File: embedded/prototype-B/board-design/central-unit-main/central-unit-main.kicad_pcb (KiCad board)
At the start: 2 copper layers, 45 x 92.5 mm, 96 parts, among them IC1 VEML6030, J1 Screw_Terminal_01x02, J2 2171790001, J3 Conn_02x05_Odd_Even, J4 Conn_ARM_JTAG_SWD_20, SW1 CAS-120TA1, U1 STM32L452RETx, U2 TPS63000, U3 MIC2778-2YM5-TR, U4 USBLC6-2SC6, U5 BQ24074RGT, U6 LIS2HH12, Y1 ECS-_327-12_5-34B-TR, Y2 STDCSU1-8M

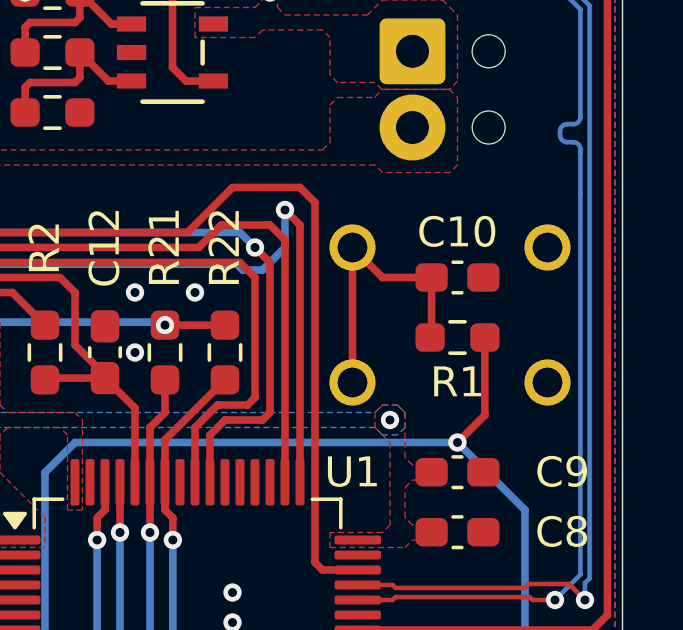
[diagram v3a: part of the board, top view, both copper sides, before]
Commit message: [Central unit] Tactile switch button wrongly routed
Fixed the MCU reset tactile switch bug.

Signed-off-by: Nicolae-Andrei Prodan <vasilenicolaeandrei@gmail.com>
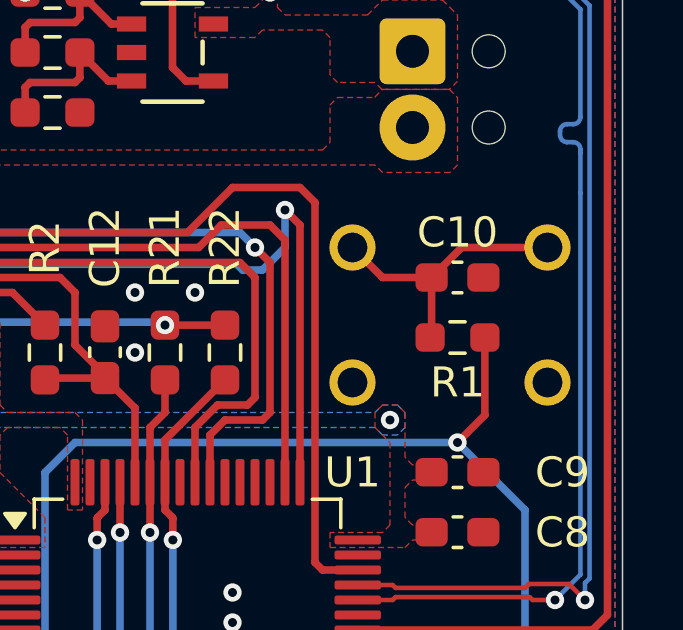
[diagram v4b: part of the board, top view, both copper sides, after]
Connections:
- C10 pad 1: Net-(S1-COM_2) -> Net-(S1-COM_1)
- R1 pad 1: Net-(S1-COM_2) -> Net-(S1-COM_1)
- S1 pad 1: GND -> Net-(S1-COM_1)
- S1 pad 2: Net-(S1-COM_2) -> Net-(S1-COM_1)
- S1 pad 4: Net-(S1-COM_2) -> GND
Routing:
- net Net-(S1-COM_2): track 9.57 -> 0.00 mm
- net Net-(S1-COM_1): track 0.00 -> 9.35 mm
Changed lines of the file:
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@@
 			(layers "F.Cu" "F.Mask" "F.Paste")
 			(roundrect_rratio 0.25)
-			(net "Net-(S1-COM_2)")
+			(net "Net-(S1-COM_1)")
 			(pintype "passive")
 		)
@@
 			(layers "F.Cu" "F.Mask" "F.Paste")
 			(roundrect_rratio 0.25)
-			(net "Net-(S1-COM_2)")
+			(net "Net-(S1-COM_1)")
 			(pintype "passive")
 		)
@@
 			(layers "*.Cu" "*.Mask")
 			(remove_unused_layers no)
-			(net "GND")
+			(net "Net-(S1-COM_1)")
 			(pinfunction "COM_1_1")
 			(pintype "passive")
@@
 			(layers "*.Cu" "*.Mask")
 			(remove_unused_layers no)
-			(net "Net-(S1-COM_2)")
+			(net "Net-(S1-COM_1)")
 			(pinfunction "COM_2_2")
 			(pintype "passive")
@@
 			(layers "*.Cu" "*.Mask")
 			(remove_unused_layers no)
-			(net "Net-(S1-COM_2)")
+			(net "GND")
 			(pinfunction "NO_2_4")
 			(pintype "passive")
@@
 	)
 	(segment
-		(start 155.5 86.5)
-		(end 155.5 91)
-		(width 0.254)
-		(locked yes)
-		(layer "F.Cu")
-		(net "Net-(S1-COM_2)")
-	)
-	(segment
-		(start 158.1375 87.5)
-		(end 158.1375 89.45)
-		(width 0.254)
-		(locked yes)
-		(layer "F.Cu")
-		(net "Net-(S1-COM_2)")
-	)
-	(segment
-		(start 158.1375 89.45)
-		(end 158.0875 89.5)
-		(width 0.254)
-		(locked yes)
-		(layer "F.Cu")
-		(net "Net-(S1-COM_2)")
-	)
-	(segment
-		(start 158.1375 87.5)
-		(end 156.5 87.5)
-		(width 0.254)
-		(locked yes)
-		(layer "F.Cu")
-		(net "Net-(S1-COM_2)")
-	)
-	(segment
-		(start 156.5 87.5)
-		(end 155.5 86.5)
-		(width 0.254)
-		(locked yes)
-		(layer "F.Cu")
-		(net "Net-(S1-COM_2)")
-	)
-	(segment
 		(start 131.5875 112)
 		(end 131.5875 117.9125)
@@
 		(net "/Connector/JTDO{slash}TRACESWO")
 	)
+	(segment
+		(start 158.1375 87.5)
+		(end 158.1375 89.45)
+		(width 0.254)
+		(layer "F.Cu")
+		(net "Net-(S1-COM_1)")
+	)
+	(segment
+		(start 159.1375 86.5)
+		(end 158.1375 87.5)
+		(width 0.254)
+		(layer "F.Cu")
+		(net "Net-(S1-COM_1)")
+	)
+	(segment
+		(start 158.1375 89.45)
+		(end 158.0875 89.5)
+		(width 0.254)
+		(layer "F.Cu")
+		(net "Net-(S1-COM_1)")
+	)
+	(segment
+		(start 162 86.5)
+		(end 159.1375 86.5)
+		(width 0.254)
+		(layer "F.Cu")
+		(net "Net-(S1-COM_1)")
+	)
+	(segment
+		(start 158.1375 87.5)
+		(end 156.5 87.5)
+		(width 0.254)
+		(layer "F.Cu")
+		(net "Net-(S1-COM_1)")
+	)
+	(segment
+		(start 156.5 87.5)
+		(end 155.5 86.5)
+		(width 0.254)
+		(layer "F.Cu")
+		(net "Net-(S1-COM_1)")
+	)
 	(zone

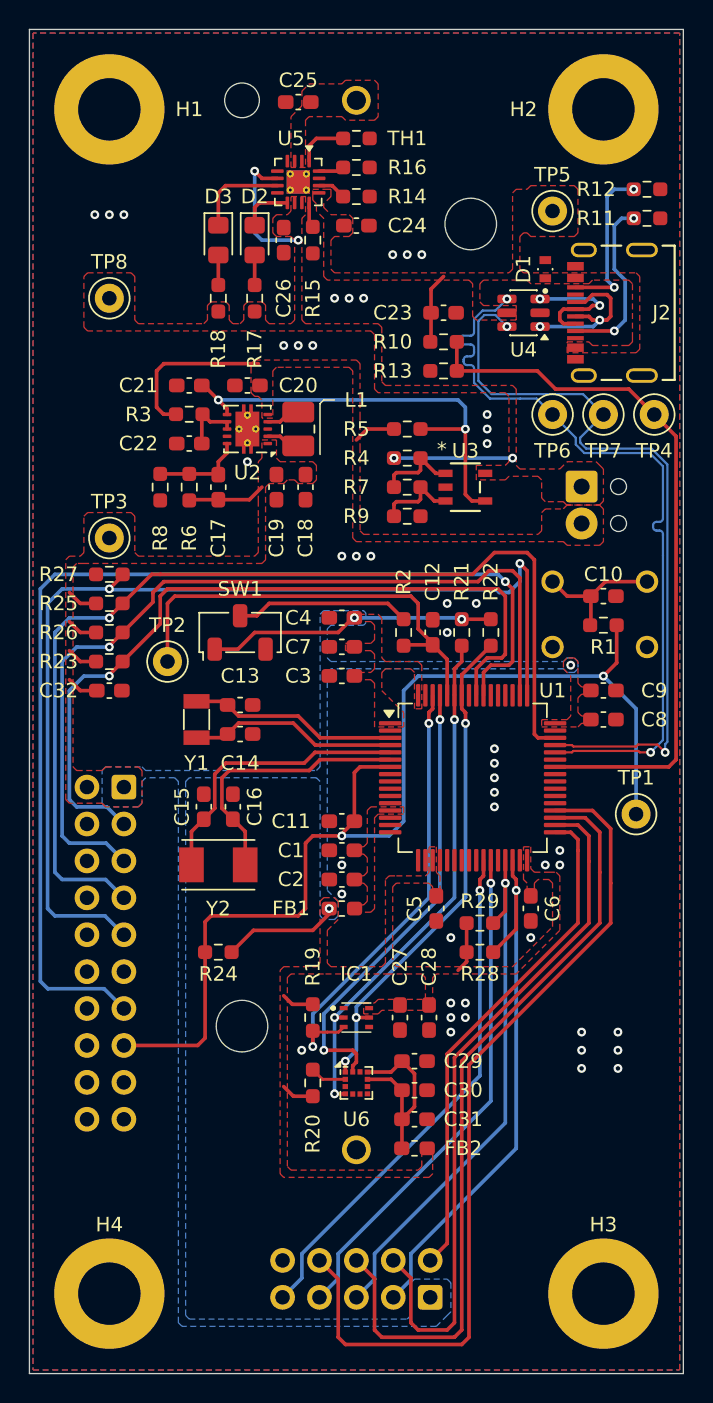
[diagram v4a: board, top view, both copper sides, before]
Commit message: [Central unit]
Integrated the LED driver into the cetral unit board.

Signed-off-by: Nicolae-Andrei Prodan <vasilenicolaeandrei@gmail.com>
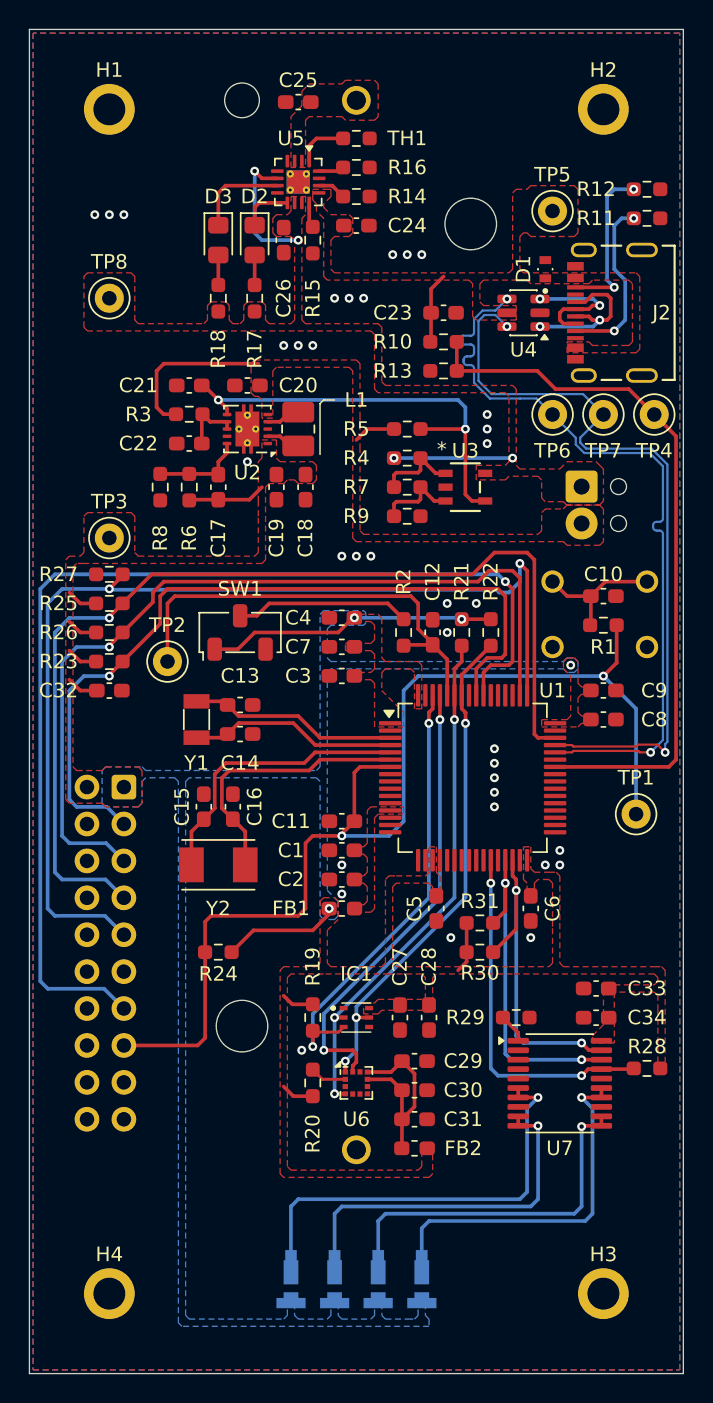
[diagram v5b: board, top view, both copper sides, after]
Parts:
- removed the J3 at (147.1, 135.8)
- added C33: 10uF/16V/10%C0603, Capacitor_SMD:C_0603_1608Metric_Pad1.08x0.95mm_HandSolder, F.Cu at (158.5, 114.5)
- added C34: 100nF/16V/10%C0603, Capacitor_SMD:C_0603_1608Metric_Pad1.08x0.95mm_HandSolder, F.Cu at (158.5, 116.5)
- added D4: MP-3014-1100-50-70, MP_3014_1100_50_70:LED_MP-3014-1100-50-70, B.Cu at (137.5, 134.5)
- added D5: MP-3014-1100-50-70, MP_3014_1100_50_70:LED_MP-3014-1100-50-70, B.Cu at (140.5, 134.5)
- added D6: MP-3014-1100-50-70, MP_3014_1100_50_70:LED_MP-3014-1100-50-70, B.Cu at (143.5, 134.5)
- added D7: MP-3014-1100-50-70, MP_3014_1100_50_70:LED_MP-3014-1100-50-70, B.Cu at (146.5, 134.5)
- added R30: 10K/0.1W/1%/R0603, Resistor_SMD:R_0603_1608Metric_Pad0.98x0.95mm_HandSolder, F.Cu at (150.5, 112.0)
- added R31: 10K/0.1W/1%/R0603, Resistor_SMD:R_0603_1608Metric_Pad0.98x0.95mm_HandSolder, F.Cu at (150.5, 110.0)
- added U7: TLC59108xPW, Package_SO:TSSOP-20_4.4x6.5mm_P0.65mm, F.Cu at (156.0, 121.0)
- H1, H2, H3, H4: footprint MountingHole:MountingHole_4.3mm_M4_ISO7380_Pad -> MountingHole:MountingHole_2.2mm_M2_ISO7380_Pad
- R28: value 4.7K/0.1W/1%/R0603 -> 10K/0.1W/1%/R0603
- R29: value 4.7K/0.1W/1%/R0603 -> 750R/0.1W/1%/R0603
- moved R28 14.0 mm to (162.0, 120.0), turned to 0 degrees
- moved R29 6.96 mm to (153.0, 116.5), turned to 0 degrees
- renumbered J4 to J3
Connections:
- R28 pad 1: /Connector/I2C_SDA -> /LED/~{RESET}
- R29 pad 1: /Connector/I2C_SCL -> Net-(U7-REXT)
- R29 pad 2: +3V3 -> GND
- U1 pad 26: /Connector/GPIO0 -> unconnected-(U1-PB0-Pad26)
- U1 pad 27: /Connector/GPIO1 -> /LED/~{RESET}
- U1 pad 29: /Connector/I2C_SCL -> /LED/I2C_SCL
- U1 pad 30: /Connector/I2C_SDA -> /LED/I2C_SDA
- U1 pad 33: /Connector/SPI_SS -> unconnected-(U1-PB12-Pad33)
- U1 pad 34: /Connector/SPI_SCK -> unconnected-(U1-PB13-Pad34)
- U1 pad 35: /Connector/SPI_MISO -> unconnected-(U1-PB14-Pad35)
- U1 pad 36: /Connector/SPI_MOSI -> unconnected-(U1-PB15-Pad36)
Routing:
- net /Connector/SPI_MOSI: track 58.6 -> 0.00 mm
- net /Connector/SPI_MISO: track 53.4 -> 0.00 mm
- net /Connector/SPI_SCK: track 48.2 -> 0.00 mm
- net /Connector/I2C_SDA: track 38.6 -> 0.00 mm, vias 1 -> 0
- net /Connector/I2C_SCL: track 37.4 -> 0.00 mm, vias 1 -> 0
- net /Connector/GPIO0: track 35.8 -> 0.00 mm, vias 1 -> 0
- net /Connector/GPIO1: track 35.0 -> 0.00 mm, vias 1 -> 0
- net /Connector/SPI_SS: track 35.0 -> 0.00 mm
- net Net-(U7-~{OUT0}): track 0.00 -> 29.7 mm, vias 0 -> 1
- net Net-(U7-~{OUT6}): track 0.00 -> 25.2 mm, vias 0 -> 1
- net Net-(U7-~{OUT2}): track 0.00 -> 25.2 mm, vias 0 -> 1
- net Net-(U7-~{OUT4}): track 0.00 -> 25.1 mm, vias 0 -> 1
- net /LED/~{RESET}: track 0.00 -> 24.6 mm, vias 0 -> 2
- net /LED/I2C_SDA: track 0.00 -> 23.4 mm, vias 0 -> 2
- net /LED/I2C_SCL: track 0.00 -> 23.2 mm, vias 0 -> 2
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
